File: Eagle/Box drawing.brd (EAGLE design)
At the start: 0 parts

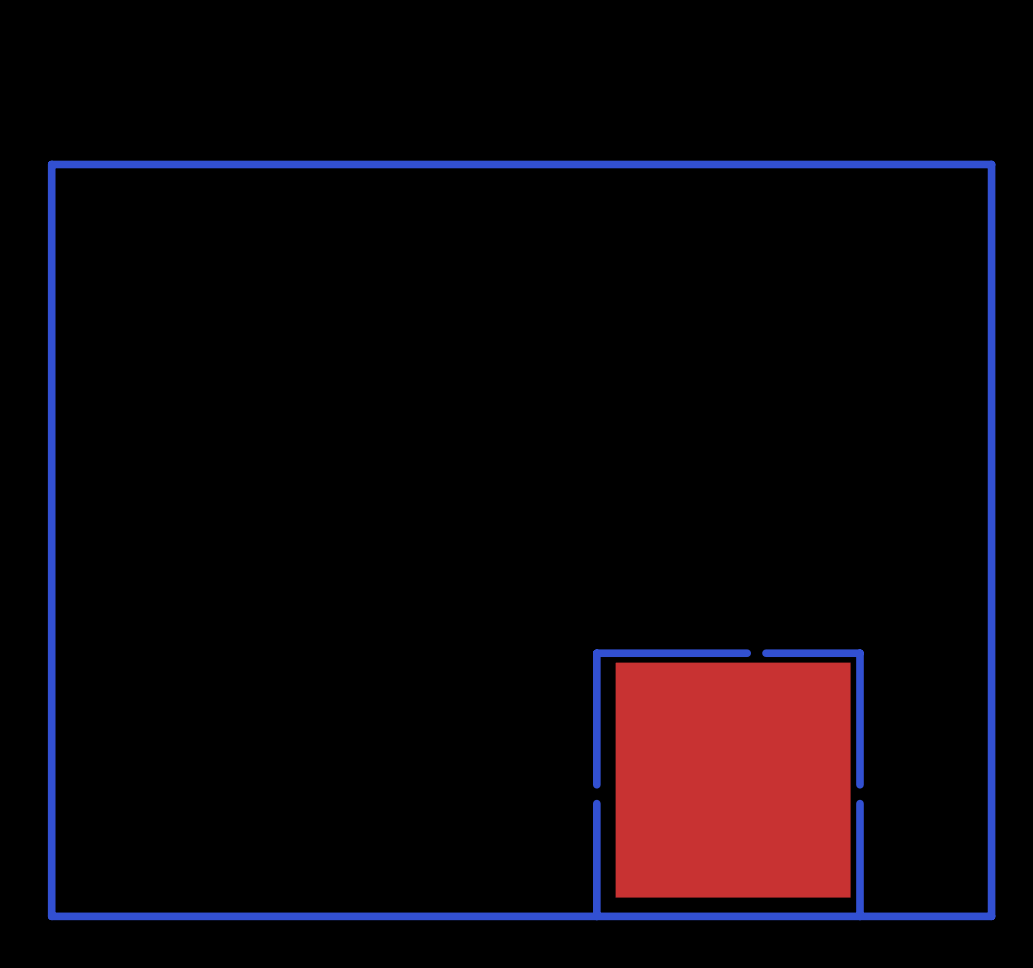
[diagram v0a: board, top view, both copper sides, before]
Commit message: Refactor the code to allow more possibilities Show linearity of the detector
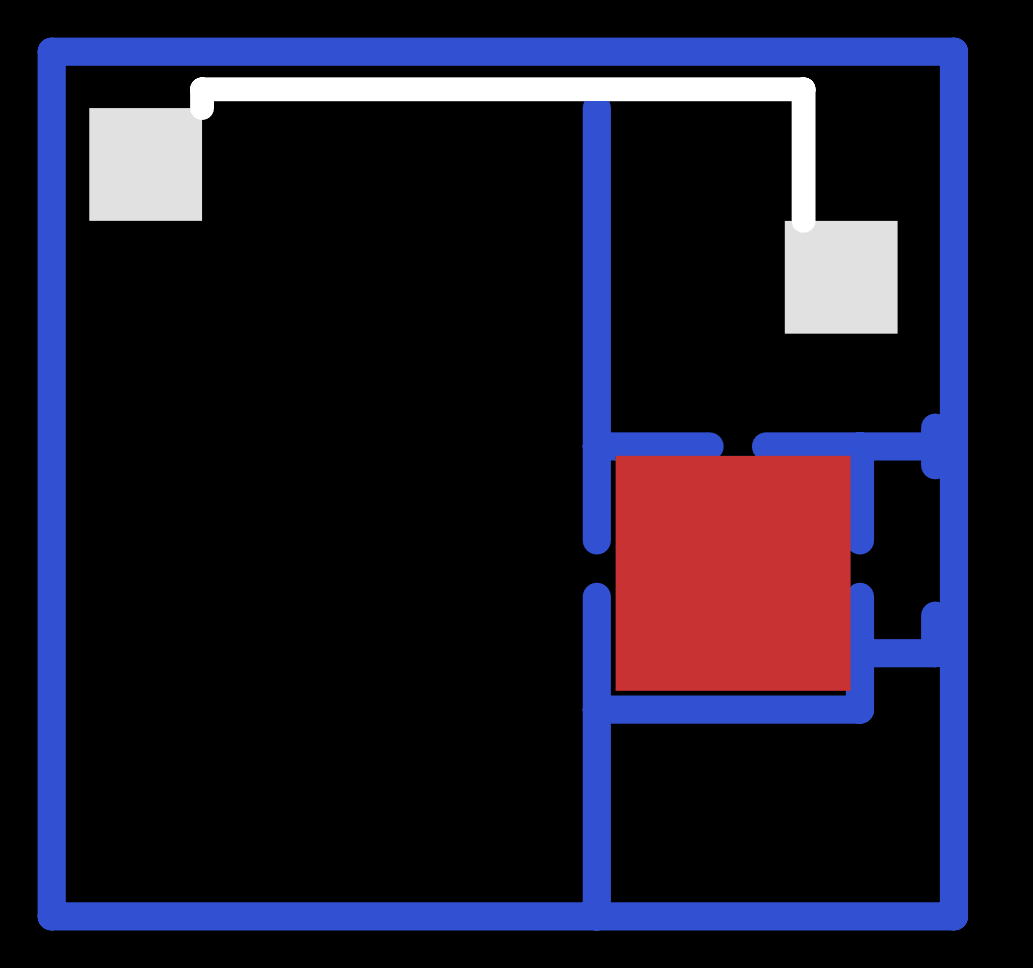
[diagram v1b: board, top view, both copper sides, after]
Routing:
- net S$1: track 192.0 -> 231.0 mm
- net S$3: track 15.0 -> 29.0 mm
- net S$2: track 12.0 -> 16.0 mm
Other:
- board outline added: 32 x 7 mm
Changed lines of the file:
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@@
 <board>
 <plain>
-<rectangle x1="30" y1="1" x2="42.5" y2="13.5" layer="1"/>
-<wire x1="44" y1="0" x2="44" y2="24" width="0.4064" layer="17"/>
-<wire x1="1" y1="0" x2="1" y2="34" width="0.4064" layer="17"/>
+<rectangle x1="30" y1="12" x2="42.5" y2="24.5" layer="1"/>
+<wire x1="45" y1="16" x2="45" y2="37" width="1.6" layer="17"/>
+<wire x1="2" y1="2" x2="2" y2="44" width="1.6" layer="17"/>
+<rectangle x1="2" y1="26" x2="7" y2="40" layer="19"/>
+<rectangle x1="39" y1="31" x2="45" y2="37" layer="21"/>
+<rectangle x1="2" y1="37" x2="8" y2="43" layer="21"/>
+<wire x1="8" y1="43" x2="8" y2="44" width="1.27" layer="20"/>
+<wire x1="8" y1="44" x2="40" y2="44" width="1.27" layer="20"/>
+<wire x1="40" y1="44" x2="40" y2="37" width="1.27" layer="20"/>
 </plain>
 <attributes>
@@
 <signals>
 <signal name="S$1">
-<wire x1="0" y1="0" x2="29" y2="0" width="0.4064" layer="16"/>
-<wire x1="29" y1="0" x2="43" y2="0" width="0.4064" layer="16"/>
-<wire x1="43" y1="0" x2="50" y2="0" width="0.4064" layer="16"/>
-<wire x1="50" y1="0" x2="50" y2="40" width="0.4064" layer="16"/>
-<wire x1="50" y1="40" x2="0" y2="40" width="0.4064" layer="16"/>
-<wire x1="0" y1="40" x2="0" y2="0" width="0.4064" layer="16"/>
-<wire x1="43" y1="0" x2="43" y2="6" width="0.4064" layer="16"/>
-<wire x1="29" y1="6" x2="29" y2="0" width="0.4064" layer="16"/>
+<wire x1="0" y1="0" x2="29" y2="0" width="1.5" layer="16"/>
+<wire x1="29" y1="0" x2="48" y2="0" width="1.5" layer="16"/>
+<wire x1="48" y1="0" x2="48" y2="46" width="1.5" layer="16"/>
+<wire x1="48" y1="46" x2="0" y2="46" width="1.5" layer="16"/>
+<wire x1="0" y1="46" x2="0" y2="0" width="1.5" layer="16"/>
+<wire x1="43" y1="11" x2="43" y2="14" width="1.5" layer="16"/>
+<wire x1="43" y1="14" x2="43" y2="17" width="1.5" layer="16"/>
+<wire x1="29" y1="17" x2="29" y2="11" width="1.5" layer="16"/>
+<wire x1="29" y1="11" x2="29" y2="0" width="1.5" layer="16"/>
+<wire x1="29" y1="11" x2="43" y2="11" width="1.5" layer="16"/>
+<wire x1="43" y1="14" x2="47" y2="14" width="1.5" layer="16"/>
+<wire x1="47" y1="14" x2="47" y2="16" width="1.5" layer="16"/>
 </signal>
 <signal name="S$2">
-<wire x1="43" y1="7" x2="43" y2="14" width="0.4064" layer="16"/>
-<wire x1="43" y1="14" x2="38" y2="14" width="0.4064" layer="16"/>
+<wire x1="43" y1="20" x2="43" y2="25" width="1.5" layer="16"/>
+<wire x1="43" y1="25" x2="38" y2="25" width="1.5" layer="16"/>
+<wire x1="43" y1="25" x2="47" y2="25" width="1.5" layer="16"/>
+<wire x1="47" y1="25" x2="47" y2="26" width="1.5" layer="16"/>
+<wire x1="47" y1="25" x2="47" y2="24" width="1.5" layer="16"/>
 </signal>
 <signal name="S$3">
-<wire x1="37" y1="14" x2="29" y2="14" width="0.4064" layer="16"/>
-<wire x1="29" y1="14" x2="29" y2="7" width="0.4064" layer="16"/>
+<wire x1="35" y1="25" x2="29" y2="25" width="1.5" layer="16"/>
+<wire x1="29" y1="25" x2="29" y2="20" width="1.5" layer="16"/>
+<wire x1="29" y1="43" x2="29" y2="25" width="1.5" layer="16"/>
 </signal>
 </signals>
